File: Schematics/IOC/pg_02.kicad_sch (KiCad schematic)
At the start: 6 parts

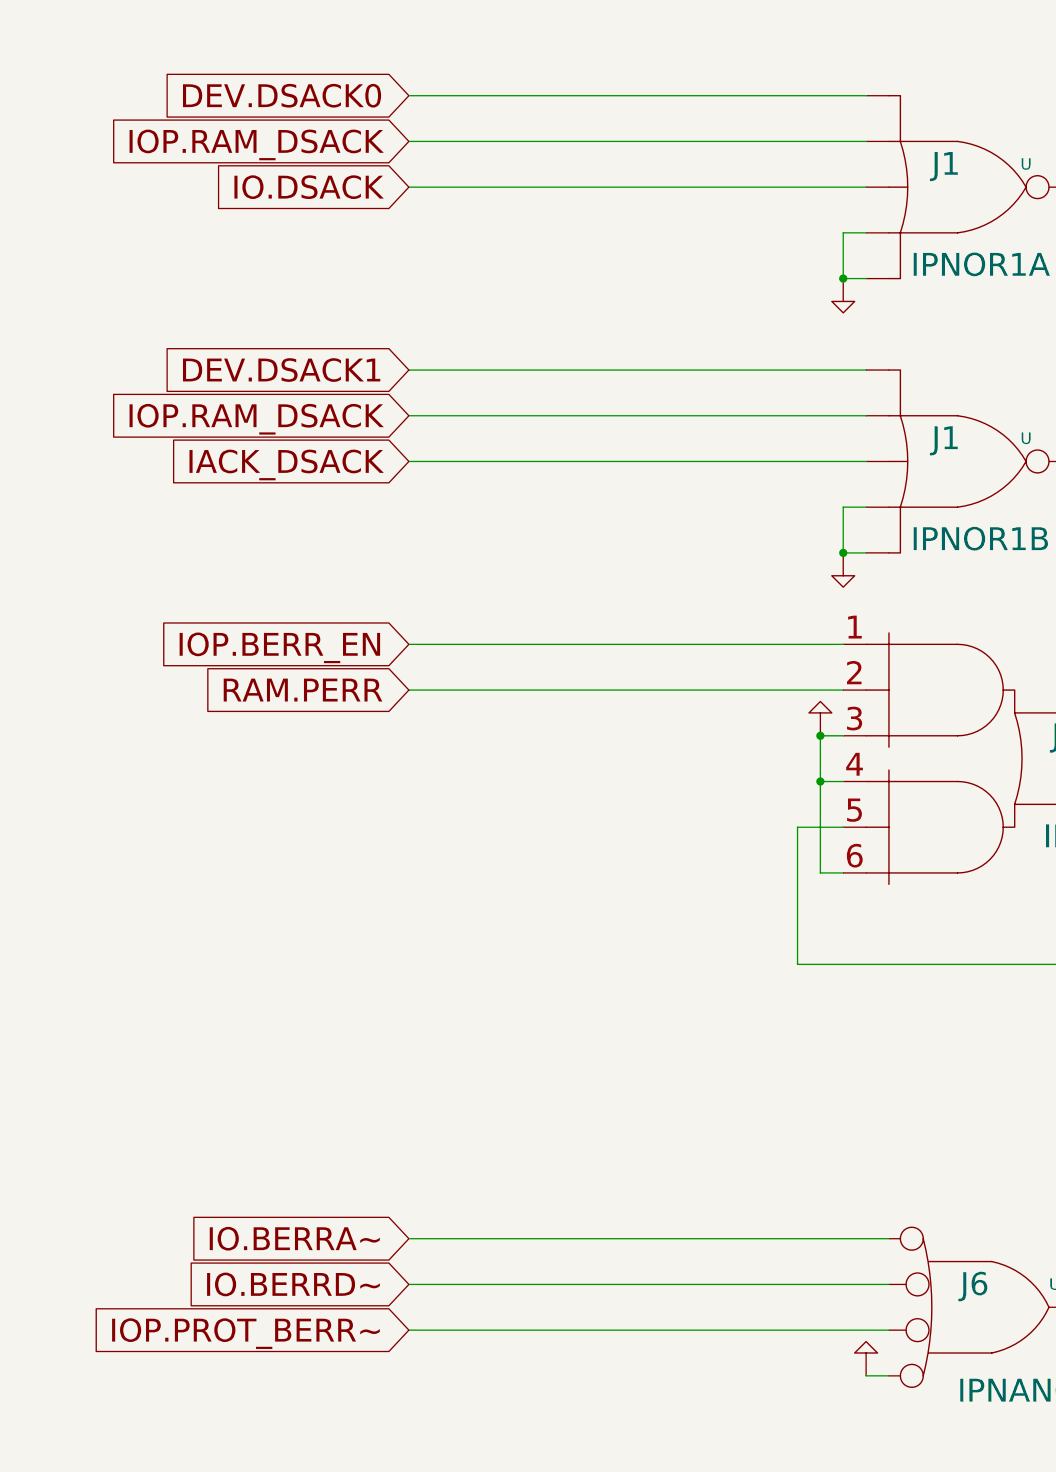
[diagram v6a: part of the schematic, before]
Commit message: Remove the UNIBUS interface.
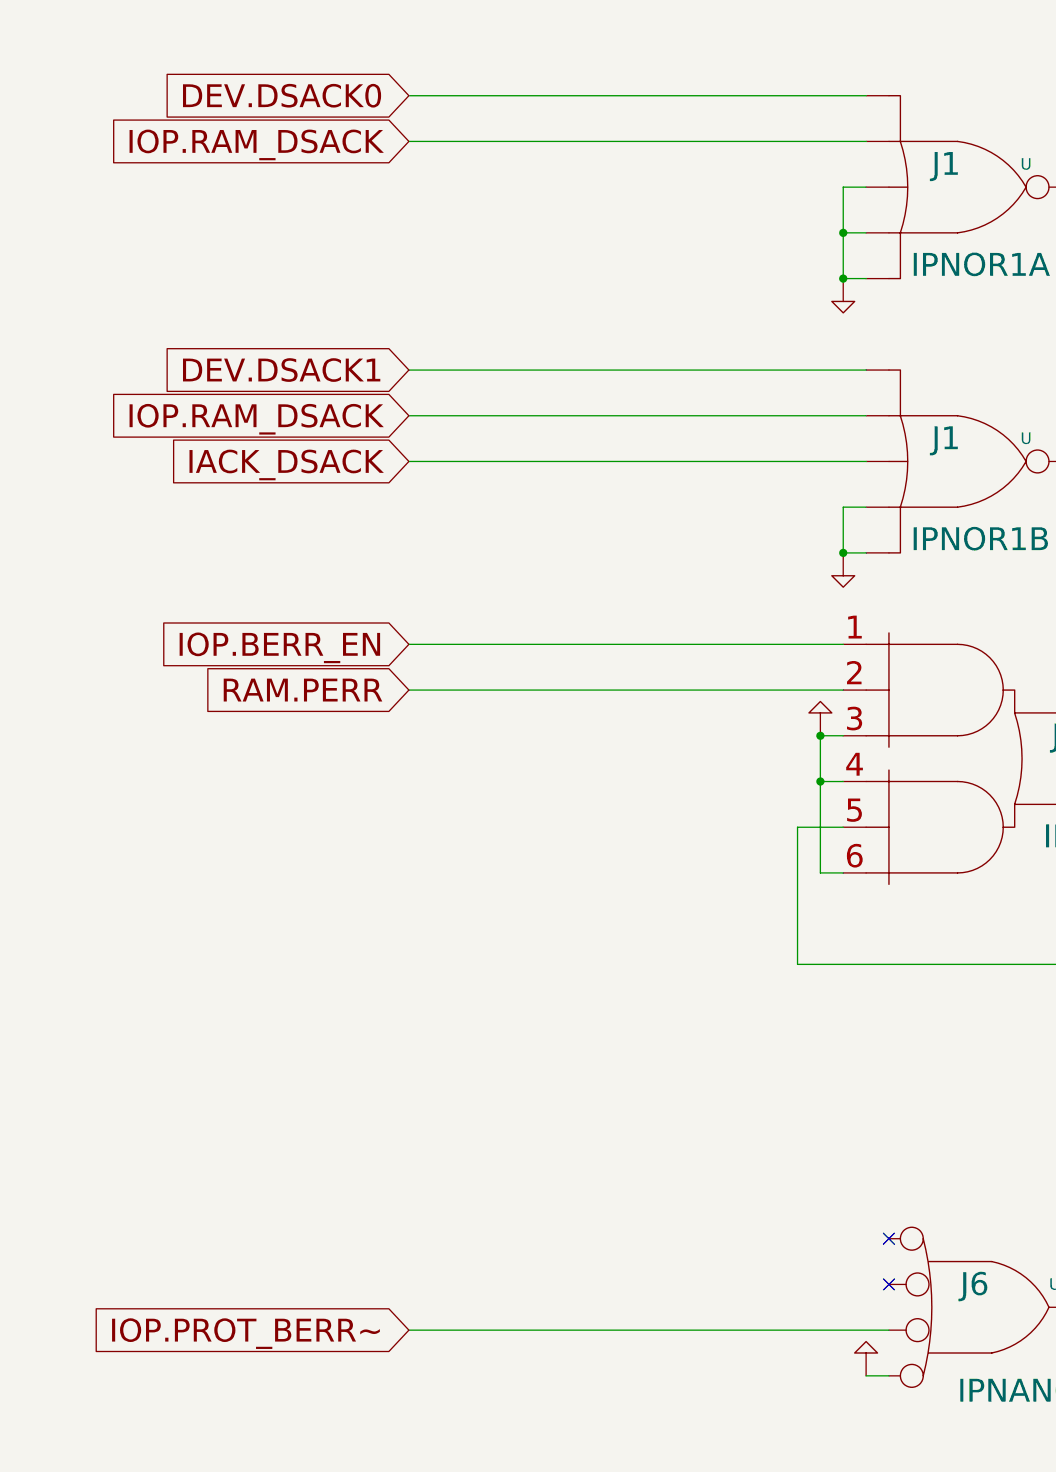
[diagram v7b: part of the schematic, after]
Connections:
- net IO.DSACK is gone; now on net PD: U.1 (D2)
- net IO.BERRA~: no longer names the net of U.1 (D0)
- net IO.BERRD~: no longer names the net of U.2 (D1)
- no-connect marks 7 -> 9
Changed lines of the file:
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@@
   (junction (at 111.76 210.82) (diameter 0) (color 0 0 0 0)
+  )
+  (junction (at 114.3 154.94) (diameter 0) (color 0 0 0 0)
   )
   (junction (at 223.52 119.38) (diameter 0) (color 0 0 0 0)
@@
   (no_connect (at 312.42 104.14))
   (no_connect (at 312.42 124.46))
+  (no_connect (at 119.38 266.7))
+  (no_connect (at 119.38 271.78))
   (no_connect (at 312.42 99.06))
   (bus_entry (at 383.54 320.04) (size -2.54 2.54)
@@
     (stroke (width 0) (type default))
   )
-  (wire (pts (xy 66.04 266.7) (xy 119.38 266.7))
-    (stroke (width 0) (type default))
-  )
   (bus (pts (xy 383.54 259.08) (xy 383.54 264.16))
     (stroke (width 0) (type default))
@@
     (stroke (width 0) (type default))
   )
+  (wire (pts (xy 114.3 149.86) (xy 114.3 154.94))
+    (stroke (width 0) (type default))
+  )
   (bus (pts (xy 383.54 274.32) (xy 383.54 279.4))
     (stroke (width 0) (type default))
@@
     (stroke (width 0) (type default))
   )
-  (wire (pts (xy 66.04 271.78) (xy 119.38 271.78))
-    (stroke (width 0) (type default))
-  )
   (wire (pts (xy 312.42 215.9) (xy 381 215.9))
     (stroke (width 0) (type default))
@@
     (stroke (width 0) (type default))
   )
-  (wire (pts (xy 66.04 149.86) (xy 116.84 149.86))
-    (stroke (width 0) (type default))
-  )
   (wire (pts (xy 175.26 165.1) (xy 231.14 165.1))
     (stroke (width 0) (type default))
@@
   )
   (wire (pts (xy 66.04 175.26) (xy 116.84 175.26))
+    (stroke (width 0) (type default))
+  )
+  (wire (pts (xy 116.84 149.86) (xy 114.3 149.86))
     (stroke (width 0) (type default))
   )
@@
     )
   )
-  (global_label "IO.BERRD~" (shape input) (at 66.04 271.78 180) (fields_autoplaced)
-    (effects (font (size 2.54 2.54)) (justify right))
-    (property "Intersheet References" "${INTERSHEET_REFS}" (id 0) (at 41.4806 271.6213 0)
-      (effects (font (size 1.905 1.905)) (justify right))
-    )
-  )
   (global_label "ECS~" (shape output) (at 391.16 119.38 0) (fields_autoplaced)
     (effects (font (size 2.54 2.54)) (justify left))
@@
     )
   )
-  (global_label "IO.DSACK" (shape input) (at 66.04 149.86 180) (fields_autoplaced)
-    (effects (font (size 2.54 2.54)) (justify right))
-    (property "Intersheet References" "${INTERSHEET_REFS}" (id 0) (at 43.5368 149.7013 0)
-      (effects (font (size 1.905 1.905)) (justify right))
-    )
-  )
   (global_label "68K.FC2" (shape output) (at 391.16 160.02 0) (fields_autoplaced)
     (effects (font (size 2.54 2.54)) (justify left))
@@
     )
   )
-  (global_label "IO.BERRA~" (shape input) (at 66.04 266.7 180) (fields_autoplaced)
-    (effects (font (size 2.54 2.54)) (justify right))
-    (property "Intersheet References" "${INTERSHEET_REFS}" (id 0) (at 41.8435 266.5413 0)
-      (effects (font (size 1.905 1.905)) (justify right))
-    )
-  )

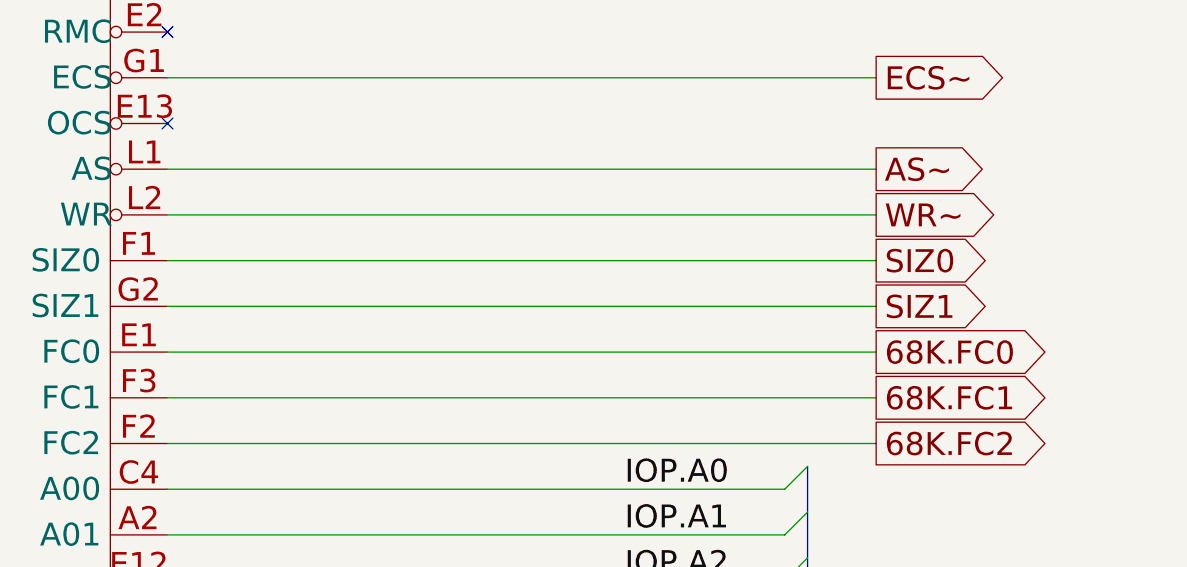
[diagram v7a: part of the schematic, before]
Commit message: IOC peel IOP access to RAM away.  Tested to 10 seconds (rc009)
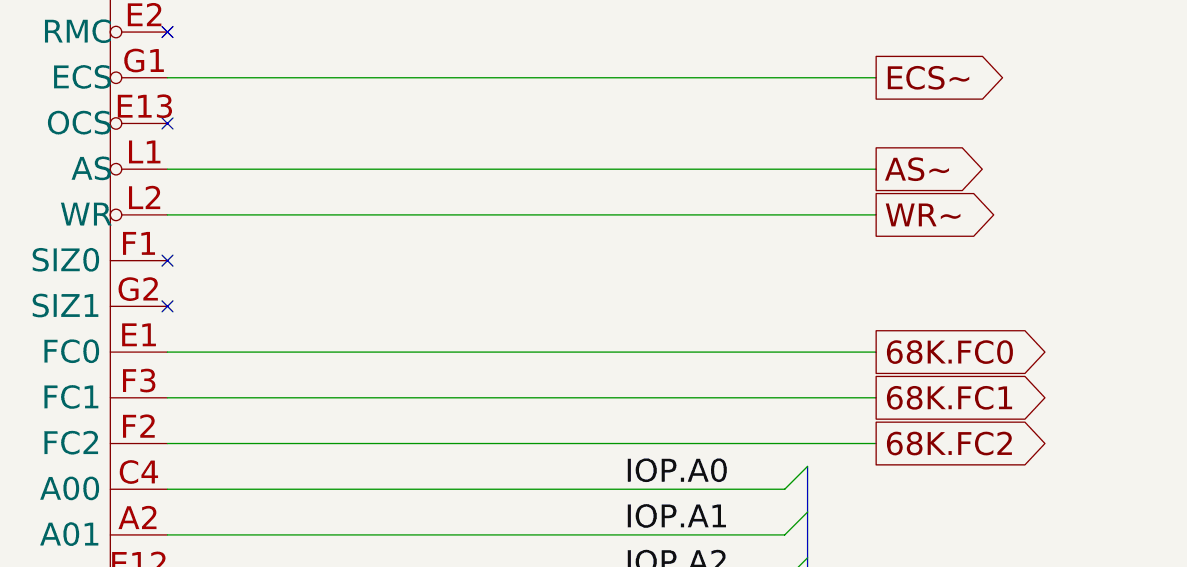
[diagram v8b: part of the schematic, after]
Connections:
- net SIZ0: no longer names the net of U.F1 (SIZ0)
- net SIZ1: no longer names the net of U.G2 (SIZ1)
- no-connect marks 9 -> 11
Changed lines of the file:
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@@
   (no_connect (at 312.42 104.14))
   (no_connect (at 312.42 124.46))
+  (no_connect (at 312.42 139.7))
+  (no_connect (at 312.42 144.78))
   (no_connect (at 119.38 266.7))
   (no_connect (at 119.38 271.78))
@@
     (stroke (width 0) (type default))
   )
-  (wire (pts (xy 312.42 139.7) (xy 391.16 139.7))
-    (stroke (width 0) (type default))
-  )
   (wire (pts (xy 114.3 154.94) (xy 114.3 160.02))
     (stroke (width 0) (type default))
@@
     (stroke (width 0) (type default))
   )
-  (wire (pts (xy 312.42 144.78) (xy 391.16 144.78))
-    (stroke (width 0) (type default))
-  )
   (wire (pts (xy 66.04 144.78) (xy 116.84 144.78))
     (stroke (width 0) (type default))
@@
   (label "IOP.A17" (at 363.22 251.46 0) (fields_autoplaced)
     (effects (font (size 2.54 2.54)) (justify left bottom))
-  )
-  (global_label "SIZ0" (shape output) (at 391.16 139.7 0) (fields_autoplaced)
-    (effects (font (size 2.54 2.54)) (justify left))
-    (property "Intersheet References" "${INTERSHEET_REFS}" (id 0) (at 404.8337 139.5413 0)
-      (effects (font (size 1.905 1.905)) (justify left))
-    )
   )
   (global_label "IOP.BERR_EN" (shape input) (at 66.04 200.66 180) (fields_autoplaced)
@@
     )
   )
-  (global_label "SIZ1" (shape output) (at 391.16 144.78 0) (fields_autoplaced)
-    (effects (font (size 2.54 2.54)) (justify left))
-    (property "Intersheet References" "${INTERSHEET_REFS}" (id 0) (at 404.8337 144.6213 0)
-      (effects (font (size 1.905 1.905)) (justify left))
-    )
-  )
